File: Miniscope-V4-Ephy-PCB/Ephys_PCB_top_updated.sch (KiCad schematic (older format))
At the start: 41 parts, among them J1 34 Circuit Slimslack Connector, J10 Conn_01x01, J11 Conn_01x01, J12 Conn_01x01, J13 Conn_01x01, J4 Conn_01x01, J5 Conn_01x01, J8 Conn_01x01, U1 ATSAME70N21A-CN, U2 RHD2132_QFN-RHD2132, U3 TLV7103318DSER, U4 TXB0304RUT, Y1 ABM8G-12.000MHZ-4Y-T3

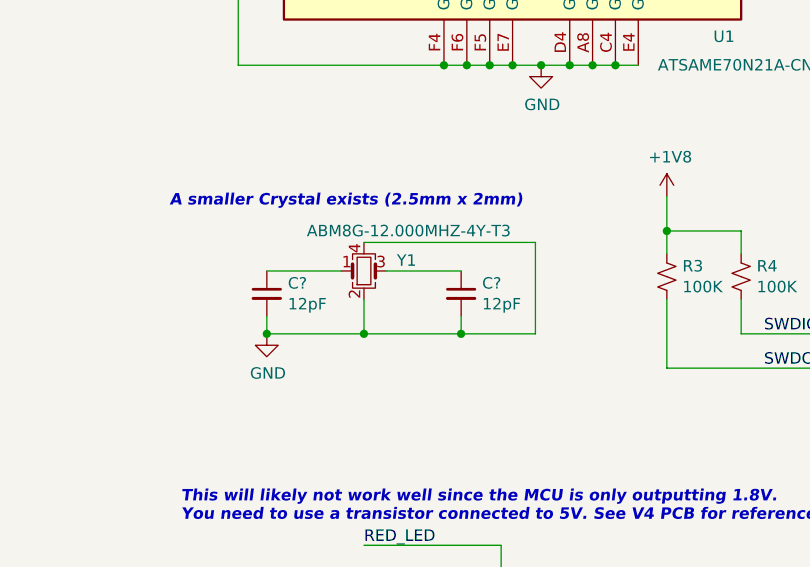
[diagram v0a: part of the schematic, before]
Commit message: Move to new KiCad project for multi-board Ephys layout
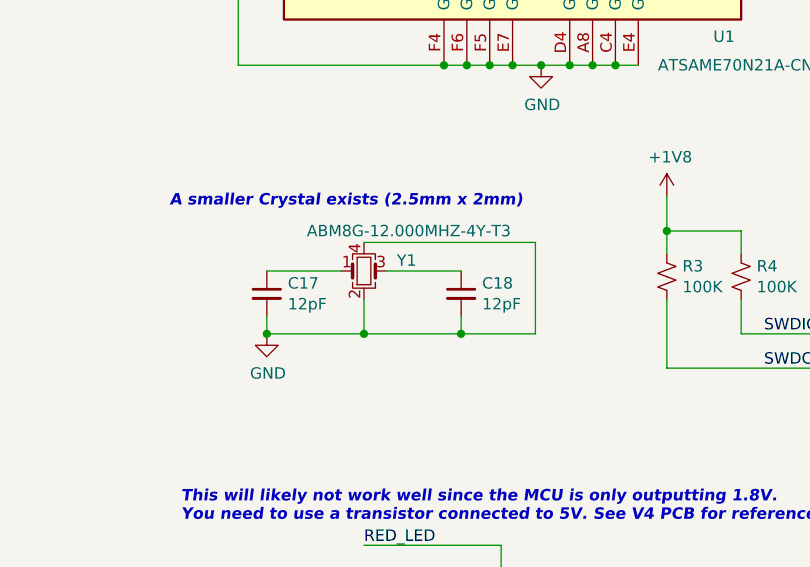
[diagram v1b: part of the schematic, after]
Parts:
- gave numbers to parts that had none: 2
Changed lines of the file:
@@
 A smaller Crystal exists (2.5mm x 2mm)
 $Comp
-L .Capacitor:GRM033R60J105MEA2D C?
+L .Capacitor:GRM033R60J105MEA2D C17
 U 1 1 5EE9363D
 P 9125 8525
-F 0 "C?" H 9217 8571 50  0000 L CNN
+F 0 "C17" H 9217 8571 50  0000 L CNN
 F 1 "GRM033R60J105MEA2D" H 8735 8695 50  0001 L CNN
 F 2 "Capacitor_SMD:C_0201_0603Metric" H 9235 8795 50  0001 C CNN
@@
 $EndComp
 $Comp
-L .Capacitor:GRM033R60J105MEA2D C?
+L .Capacitor:GRM033R60J105MEA2D C18
 U 1 1 5EE95181
 P 9975 8525
-F 0 "C?" H 10067 8571 50  0000 L CNN
+F 0 "C18" H 10067 8571 50  0000 L CNN
 F 1 "GRM033R60J105MEA2D" H 9585 8695 50  0001 L CNN
 F 2 "Capacitor_SMD:C_0201_0603Metric" H 10085 8795 50  0001 C CNN
